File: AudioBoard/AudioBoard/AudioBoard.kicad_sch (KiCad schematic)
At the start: 0 parts

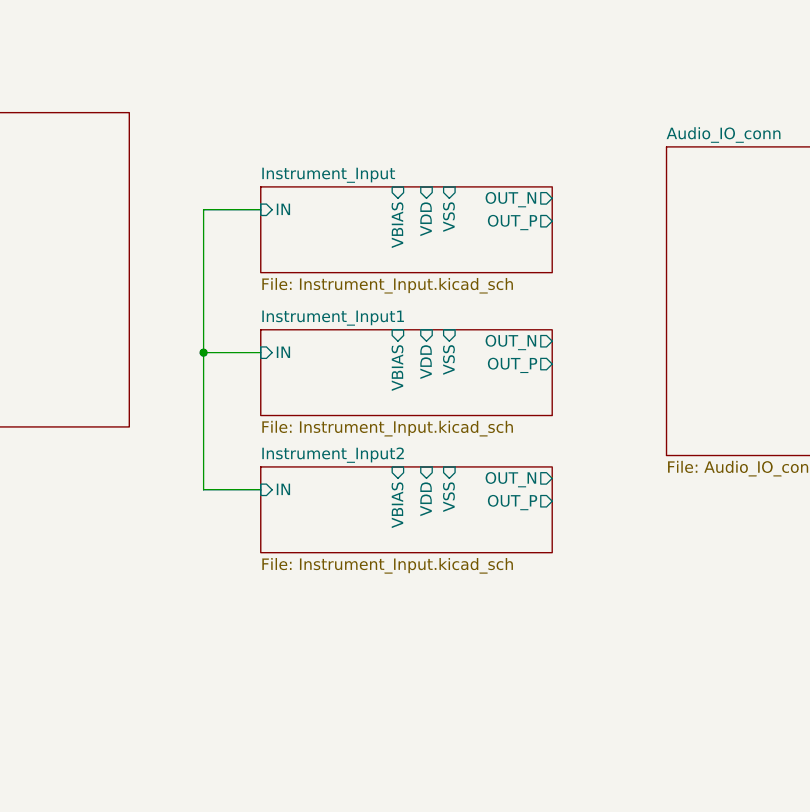
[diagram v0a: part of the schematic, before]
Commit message: added input section
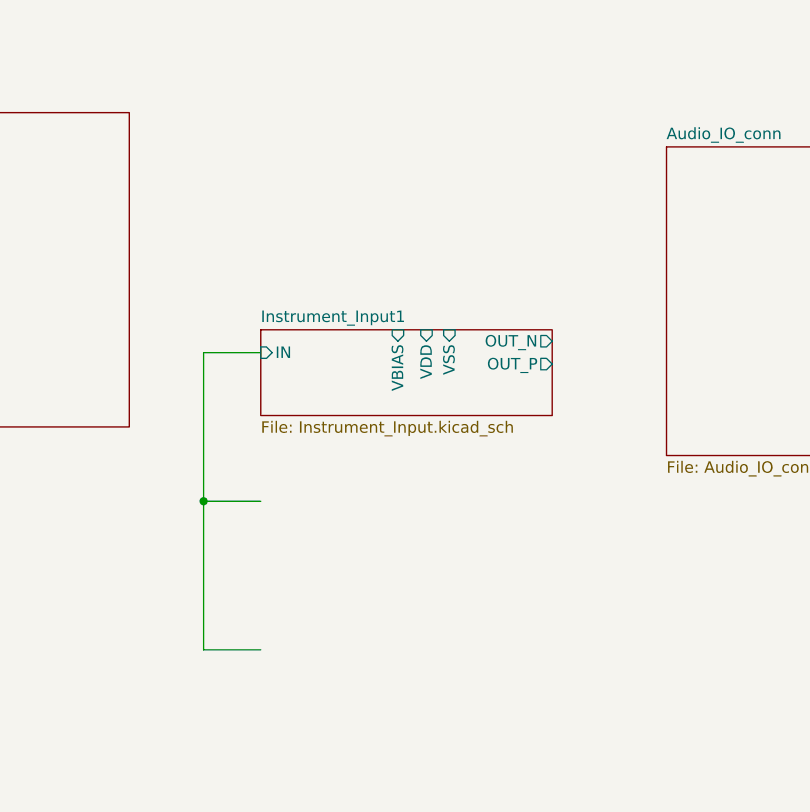
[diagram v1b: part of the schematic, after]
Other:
- removed sheet Instrument_Input
- removed sheet Instrument_Input2
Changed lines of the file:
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@@
 	(paper "A4")
 	(junction
-		(at 179.705 82.55)
+		(at 179.705 99.06)
 		(diameter 0)
 		(color 0 0 0 0)
@@
 	(wire
 		(pts
-			(xy 179.705 66.675) (xy 179.705 82.55)
+			(xy 179.705 99.06) (xy 186.055 99.06)
 		)
 		(stroke
@@
 	(wire
 		(pts
-			(xy 179.705 97.79) (xy 179.705 82.55)
+			(xy 179.705 82.55) (xy 179.705 99.06)
 		)
 		(stroke
@@
 	(wire
 		(pts
-			(xy 186.055 97.79) (xy 179.705 97.79)
+			(xy 179.705 115.57) (xy 186.055 115.57)
 		)
 		(stroke
@@
 	(wire
 		(pts
-			(xy 186.055 66.675) (xy 179.705 66.675)
+			(xy 179.705 99.06) (xy 179.705 115.57)
 		)
 		(stroke
@@
 	)
 	(sheet
-		(at 186.055 95.25)
-		(size 32.385 9.525)
-		(exclude_from_sim no)
-		(in_bom yes)
-		(on_board yes)
-		(dnp no)
-		(fields_autoplaced yes)
-		(stroke
-			(width 0.1524)
-			(type solid)
-		)
-		(fill
-			(color 0 0 0 0)
-		)
-		(property "Sheetname" "Instrument_Input2"
-			(at 186.055 94.5384 0)
-			(show_name no)
-			(do_not_autoplace no)
-			(effects
-				(font
-					(size 1.27 1.27)
-				)
-				(justify left bottom)
-			)
-		)
-		(property "Sheetfile" "Instrument_Input.kicad_sch"
-			(at 186.055 105.3596 0)
-			(show_name no)
-			(do_not_autoplace no)
-			(effects
-				(font
-					(size 1.27 1.27)
-				)
-				(justify left top)
-			)
-		)
-		(pin "IN" input
-			(at 186.055 97.79 180)
-			(effects
-				(font
-					(size 1.27 1.27)
-				)
-				(justify left)
-			)
-		)
-		(pin "OUT_N" output
-			(at 218.44 96.52 0)
-			(effects
-				(font
-					(size 1.27 1.27)
-				)
-				(justify right)
-			)
-		)
-		(pin "OUT_P" output
-			(at 218.44 99.06 0)
-			(effects
-				(font
-					(size 1.27 1.27)
-				)
-				(justify right)
-			)
-		)
-		(pin "VBIAS" input
-			(at 201.295 95.25 90)
-			(effects
-				(font
-					(size 1.27 1.27)
-				)
-				(justify right)
-			)
-		)
-		(pin "VDD" input
-			(at 204.47 95.25 90)
-			(effects
-				(font
-					(size 1.27 1.27)
-				)
-				(justify right)
-			)
-		)
-		(pin "VSS" input
-			(at 207.01 95.25 90)
-			(effects
-				(font
-					(size 1.27 1.27)
-				)
-				(justify right)
-			)
-		)
-		(instances
-			(project "AudioBoard"
-				(path "/dd5d876d-fff7-4cb4-baee-a023036d12ae"
-					(page "8")
-				)
-			)
-		)
-	)
-	(sheet
 		(at 231.14 59.69)
 		(size 22.86 34.29)
@@
 				)
 			)
-		)
-	)
-	(sheet
-		(at 186.055 64.135)
-		(size 32.385 9.525)
-		(exclude_from_sim no)
-		(in_bom yes)
-		(on_board yes)
-		(dnp no)
-		(fields_autoplaced yes)
-		(stroke
-			(width 0.1524)
-			(type solid)
-		)
-		(fill
-			(color 0 0 0 0)
-		)
-		(property "Sheetname" "Instrument_Input"
-			(at 186.055 63.4234 0)
-			(show_name no)
-			(do_not_autoplace no)
-			(effects
-				(font
-					(size 1.27 1.27)
-				)
-				(justify left bottom)
-			)
-		)
-		(property "Sheetfile" "Instrument_Input.kicad_sch"
-			(at 186.055 74.2446 0)
-			(show_name no)
-			(do_not_autoplace no)
-			(effects
-				(font
-					(size 1.27 1.27)
-				)
-				(justify left top)
-			)
-		)
-		(pin "IN" input
-			(at 186.055 66.675 180)
-			(effects
-				(font
-					(size 1.27 1.27)
-				)
-				(justify left)
-			)
-		)
-		(pin "OUT_N" output
-			(at 218.44 65.405 0)
-			(effects
-				(font
-					(size 1.27 1.27)
-				)
-				(justify right)
-			)
-		)
-		(pin "OUT_P" output
-			(at 218.44 67.945 0)
-			(effects
-				(font
-					(size 1.27 1.27)
-				)
-				(justify right)
-			)
-		)
-		(pin "VBIAS" input
-			(at 201.295 64.135 90)
-			(effects
-				(font
-					(size 1.27 1.27)
-				)
-				(justify right)
-			)
-		)
-		(pin "VDD" input
-			(at 204.47 64.135 90)
-			(effects
-				(font
-					(size 1.27 1.27)
-				)
-				(justify right)
-			)
-		)
-		(pin "VSS" input
-			(at 207.01 64.135 90)
-			(effects
-				(font
-					(size 1.27 1.27)
-				)
-				(justify right)
-			)
-		)
-		(instances
-			(project "AudioBoard"
-				(path "/dd5d876d-fff7-4cb4-baee-a023036d12ae"
-					(page "6")
-				)
-			)

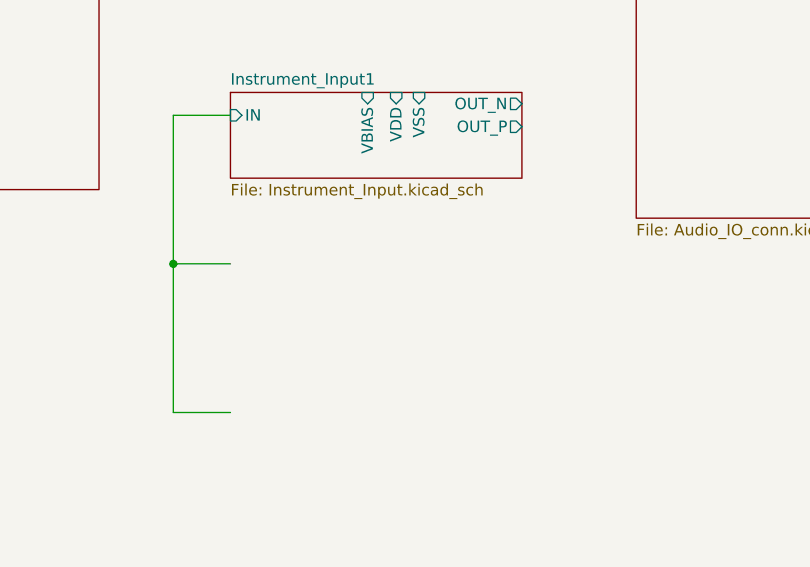
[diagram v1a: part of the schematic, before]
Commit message: input section with templates are working
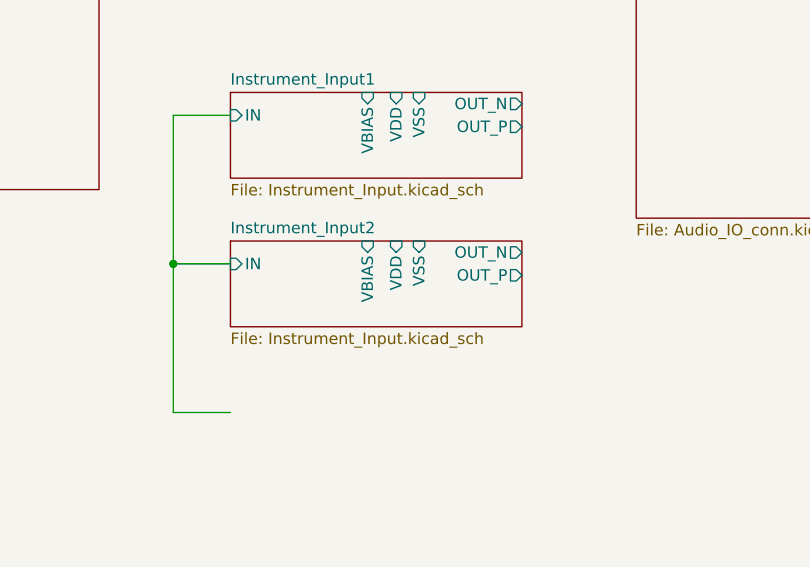
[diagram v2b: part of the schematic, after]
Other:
- added sheet Instrument_Input2 (Instrument_Input.kicad_sch)
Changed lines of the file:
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@@
+	)
+	(sheet
+		(at 186.055 96.52)
+		(size 32.385 9.525)
+		(exclude_from_sim no)
+		(in_bom yes)
+		(on_board yes)
+		(dnp no)
+		(fields_autoplaced yes)
+		(stroke
+			(width 0.1524)
+			(type solid)
+		)
+		(fill
+			(color 0 0 0 0)
+		)
+		(property "Sheetname" "Instrument_Input2"
+			(at 186.055 95.8084 0)
+			(show_name no)
+			(do_not_autoplace no)
+			(effects
+				(font
+					(size 1.27 1.27)
+				)
+				(justify left bottom)
+			)
+		)
+		(property "Sheetfile" "Instrument_Input.kicad_sch"
+			(at 186.055 106.6296 0)
+			(show_name no)
+			(do_not_autoplace no)
+			(effects
+				(font
+					(size 1.27 1.27)
+				)
+				(justify left top)
+			)
+		)
+		(pin "IN" input
+			(at 186.055 99.06 180)
+			(effects
+				(font
+					(size 1.27 1.27)
+				)
+				(justify left)
+			)
+		)
+		(pin "OUT_N" output
+			(at 218.44 97.79 0)
+			(effects
+				(font
+					(size 1.27 1.27)
+				)
+				(justify right)
+			)
+		)
+		(pin "OUT_P" output
+			(at 218.44 100.33 0)
+			(effects
+				(font
+					(size 1.27 1.27)
+				)
+				(justify right)
+			)
+		)
+		(pin "VBIAS" input
+			(at 201.295 96.52 90)
+			(effects
+				(font
+					(size 1.27 1.27)
+				)
+				(justify right)
+			)
+		)
+		(pin "VDD" input
+			(at 204.47 96.52 90)
+			(effects
+				(font
+					(size 1.27 1.27)
+				)
+				(justify right)
+			)
+		)
+		(pin "VSS" input
+			(at 207.01 96.52 90)
+			(effects
+				(font
+					(size 1.27 1.27)
+				)
+				(justify right)
+			)
+		)
+		(instances
+			(project "AudioBoard"
+				(path "/dd5d876d-fff7-4cb4-baee-a023036d12ae"
+					(page "6")
+				)
+			)
+		)
 	)
 	(sheet

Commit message: Created input sections
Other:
- added sheet Instrument_Input3 (Instrument_Input.kicad_sch)
- added sheet Instrument_Input4 (Instrument_Input.kicad_sch)
- sheet Instrument_Input1 ports: added AVDD; removed none
- sheet Instrument_Input2 ports: added AVDD; removed none
- sheet codec ports: added AVDD, DVDD, I2S{WS,CLK,SDI,SDO}, IN1_N, IN1_P, IN2_N, IN2_P, IN3_N, IN3_P, IN4_N, IN4_P, OUT1_N, OUT1_P, OUT2_N, OUT2_P, OUT3_N, OUT3_P, OUT4_N, OUT4_P, OUT5_N, OUT5_P, OUT6_N, OUT6_P, OUT7_N, OUT7_P, OUT8_N, OUT8_P, SPI{CS,CLK,MISO,MOSI}, VBIAS; removed none
- sheet power ports: added AVDD, DVDD, VDD, VSS; removed none

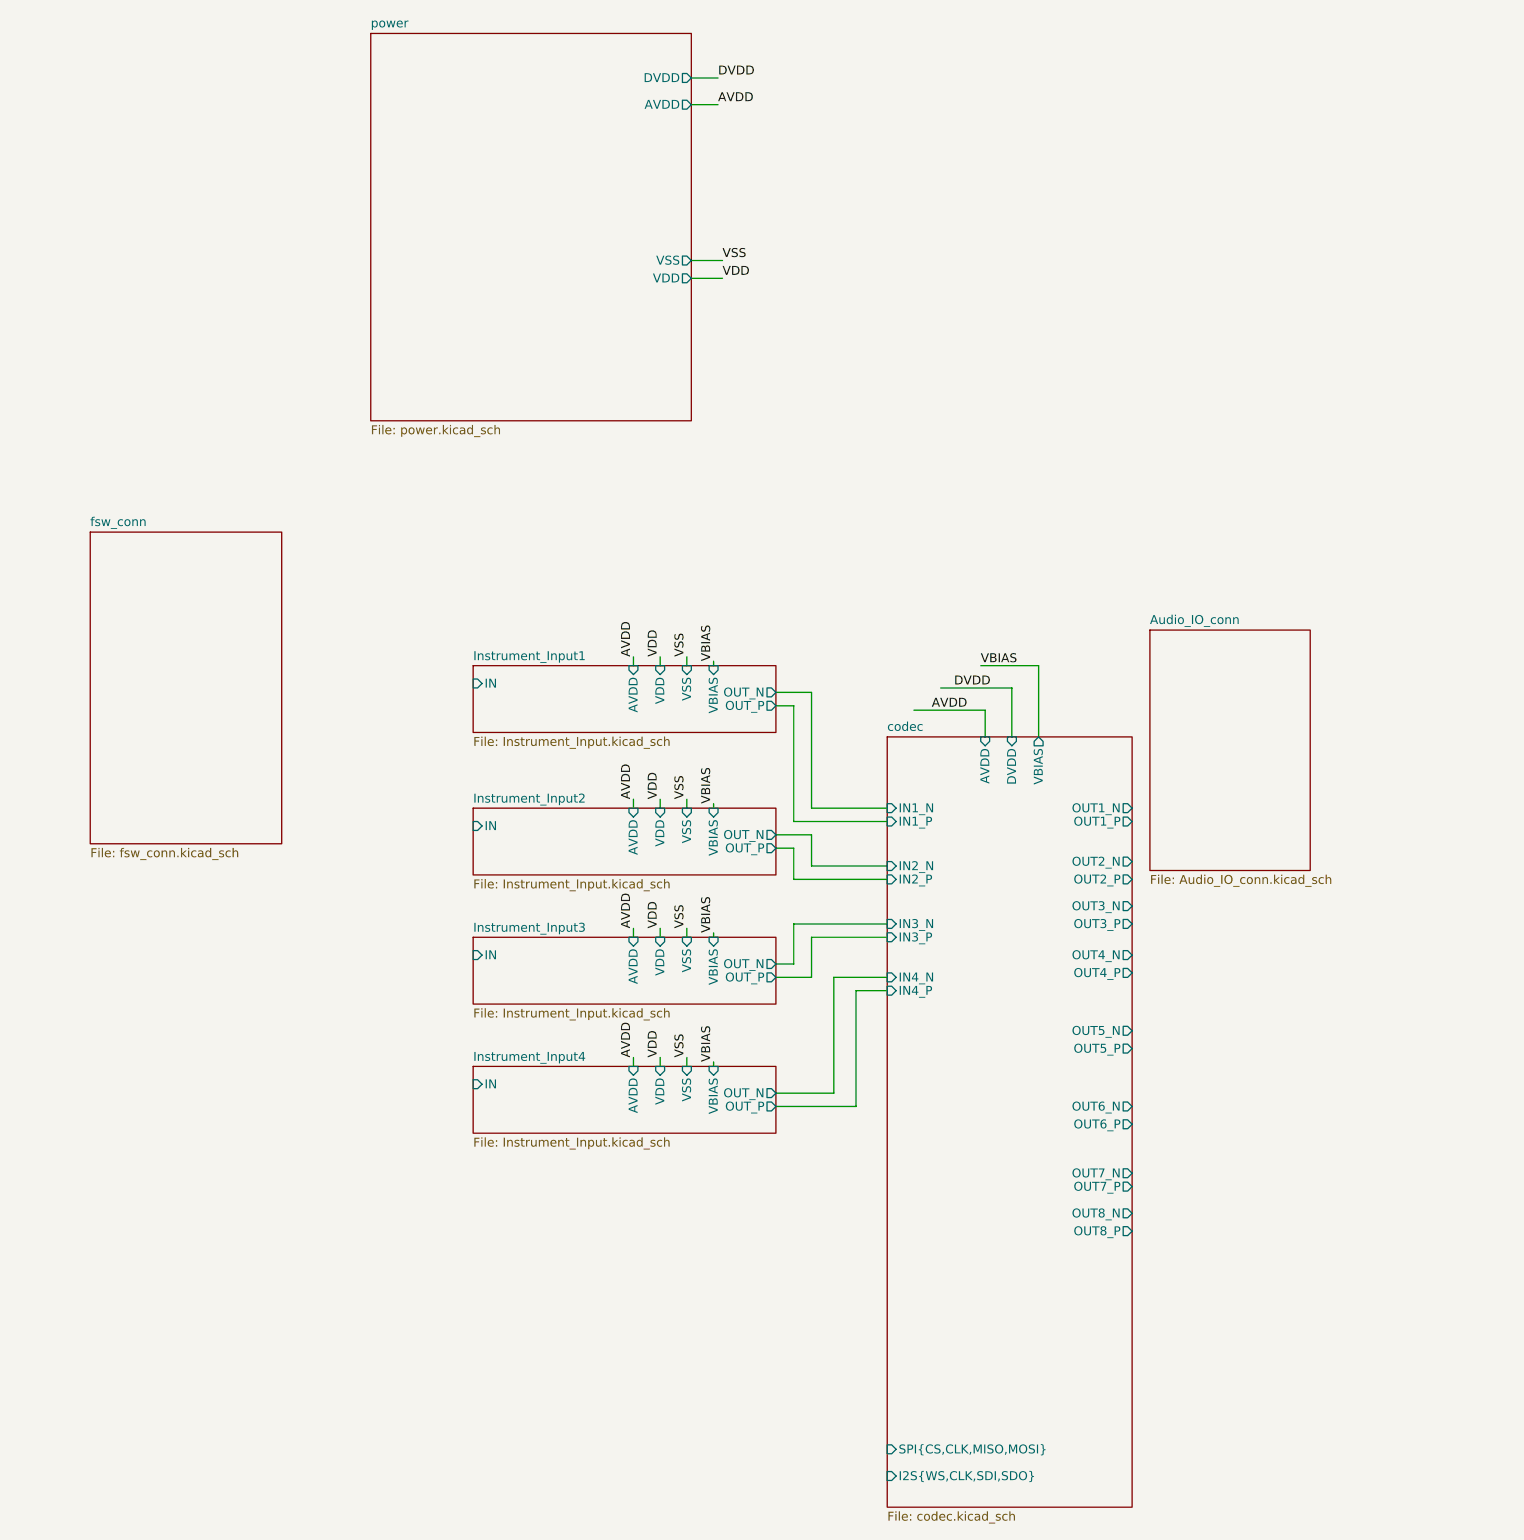
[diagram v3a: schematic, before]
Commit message: added microphone preamp
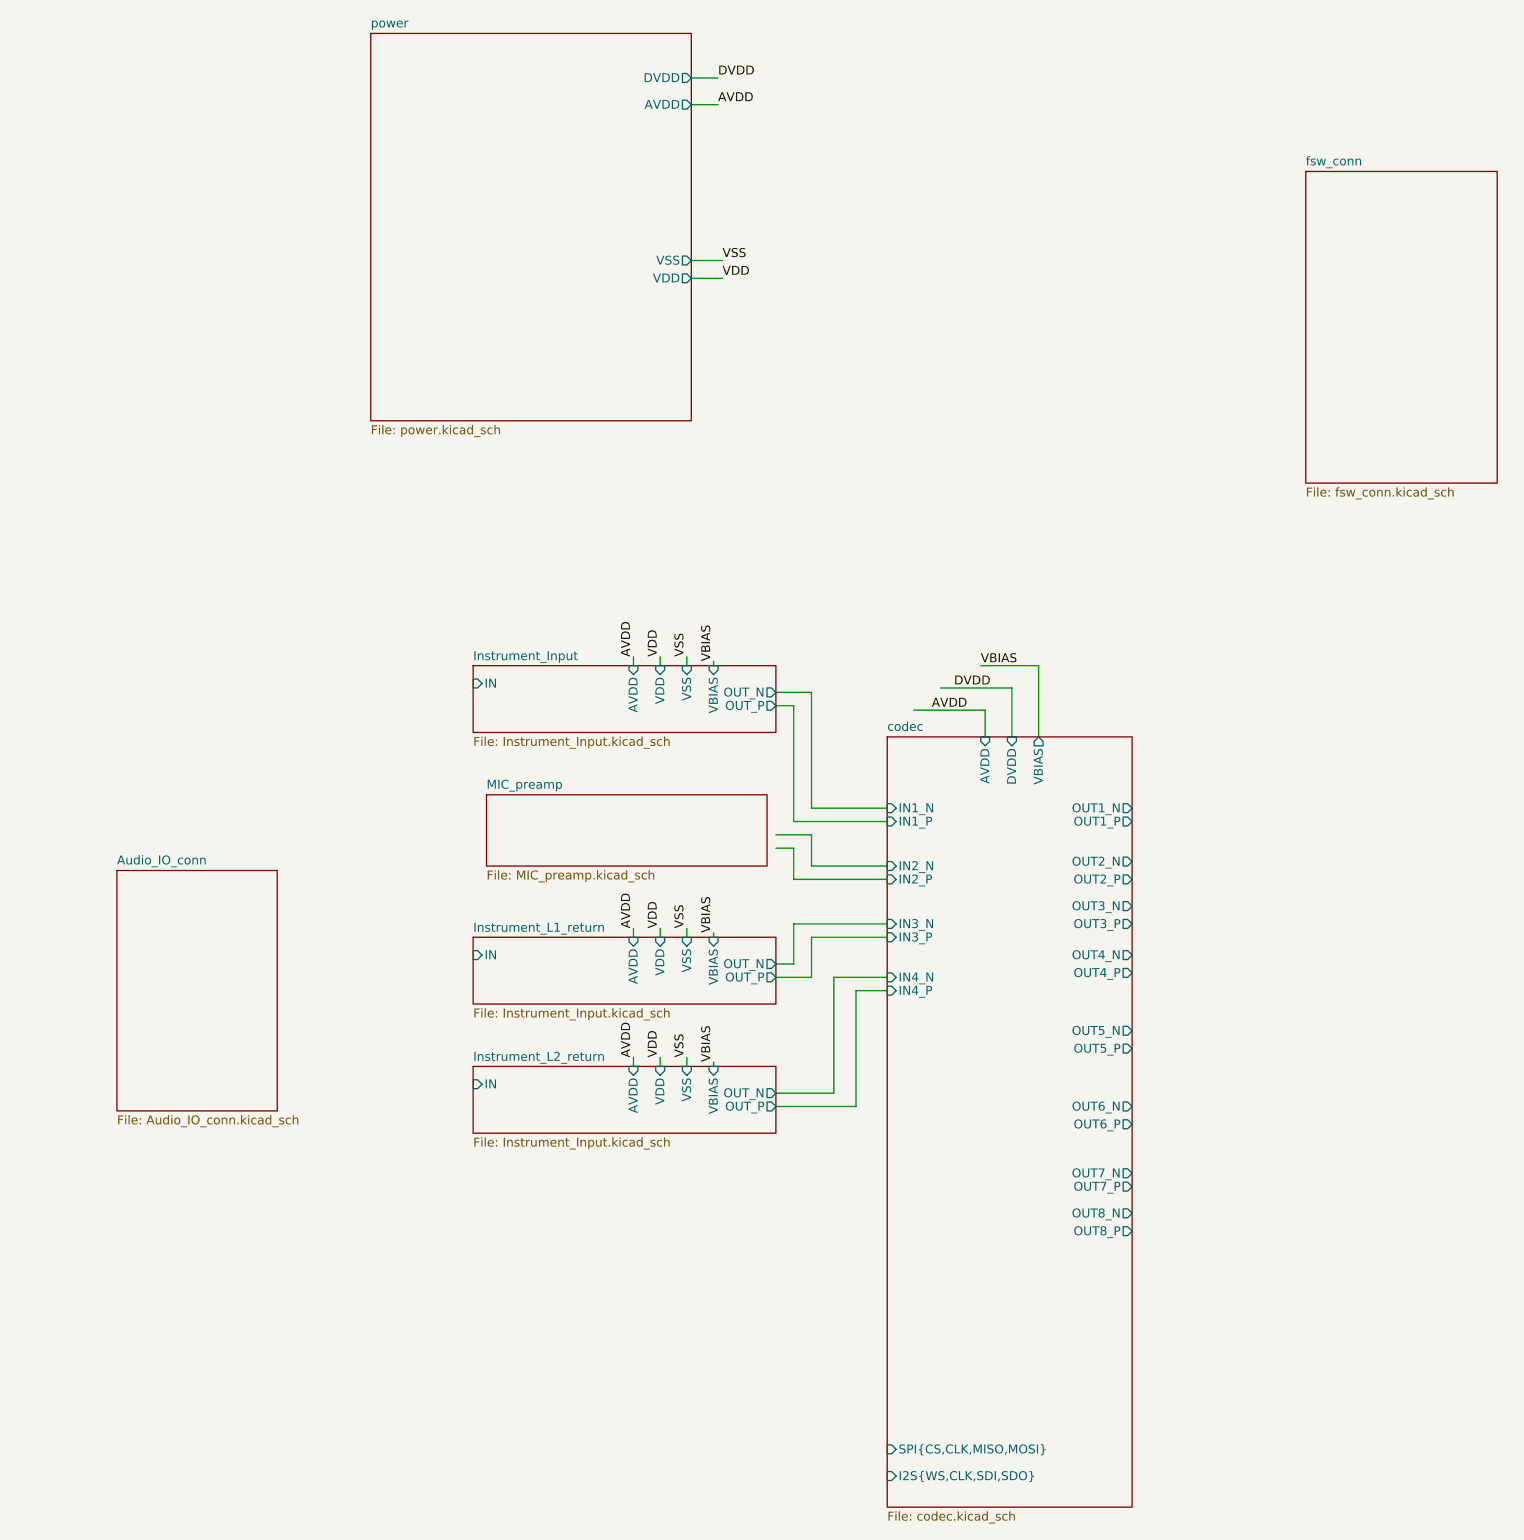
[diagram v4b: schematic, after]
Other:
- sheet Instrument_Input1 renamed Instrument_Input
- removed sheet Instrument_Input2
- removed sheet Instrument_Input3
- removed sheet Instrument_Input4
- added sheet Instrument_L1_return (Instrument_Input.kicad_sch)
- added sheet Instrument_L2_return (Instrument_Input.kicad_sch)
- added sheet MIC_preamp (MIC_preamp.kicad_sch)
